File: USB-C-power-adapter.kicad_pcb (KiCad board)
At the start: 2 copper layers, 21.1 x 40.1 mm, 60 parts, among them J1 USB-C_GCT_USB4105-GF-A, J2 JST_SH_1x4_SM04B-SRSS-TB-LF-SN, J4 Molex_Nano-Fit_1x2_105313-220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, Q1 SQS401EN-T1_BE3, U1 TPD4E02B04DQA, U2 SIC477ED-T1-GE3, U3 STUSB4500_QFN, U4 TPD4E02B04DQA

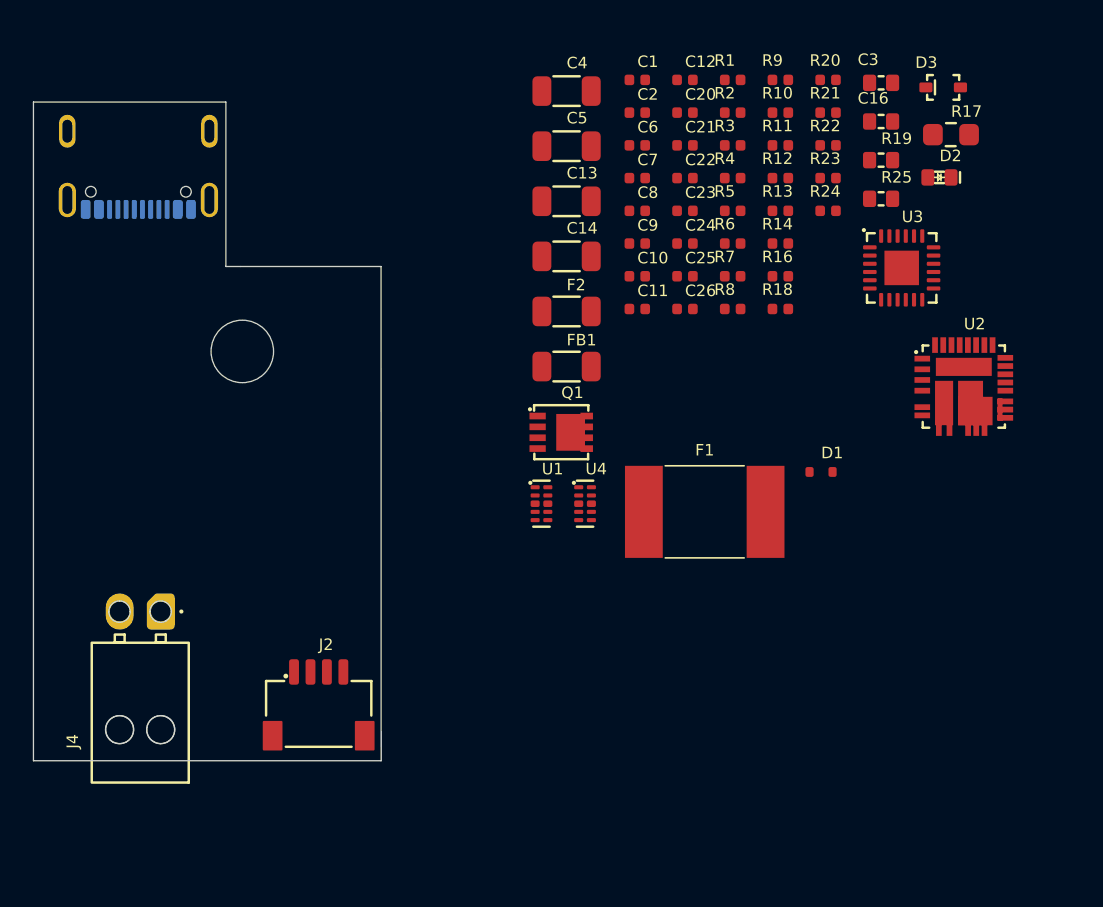
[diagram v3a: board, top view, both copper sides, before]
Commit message: [#57225] Placement of buck converter
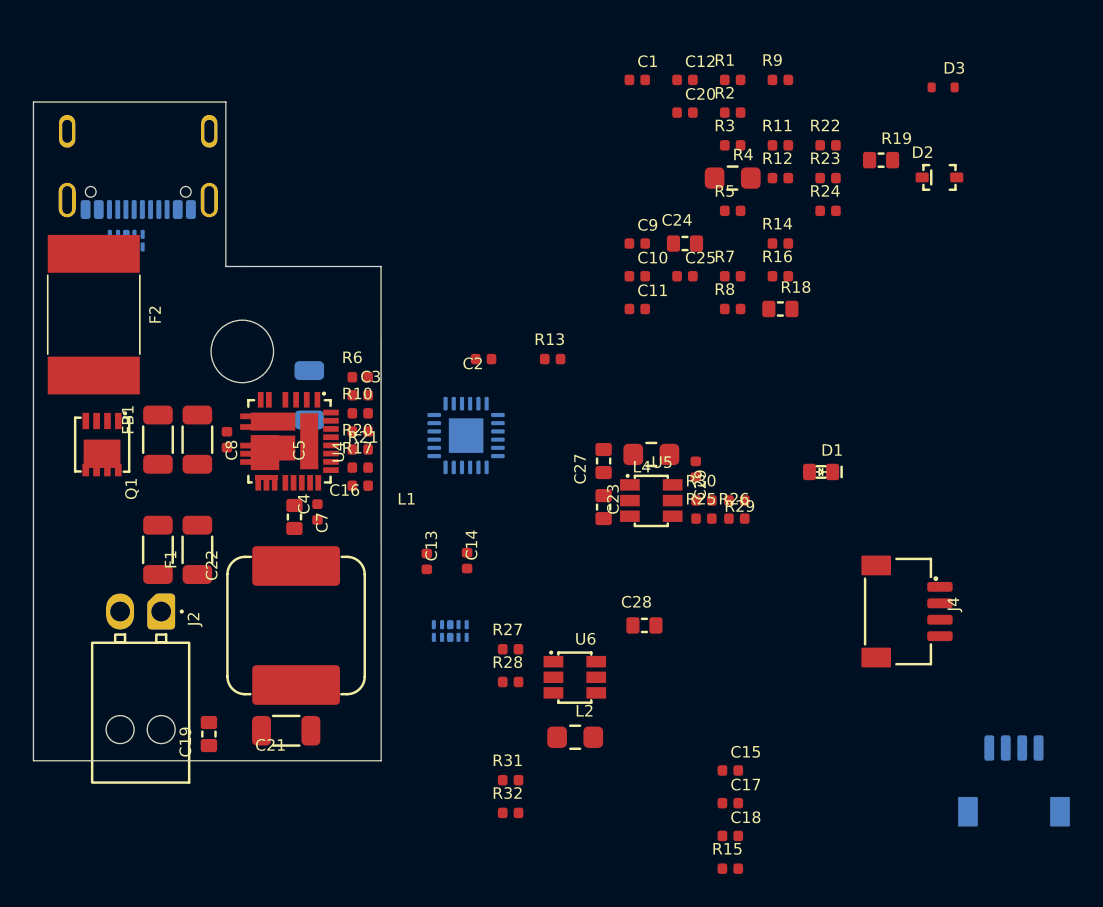
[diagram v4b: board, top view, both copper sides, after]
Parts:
- removed C26: C_1u_0402, antmicro-footprints:C_0402_1005Metric
- added C15: C_1u_0402, antmicro-footprints:C_0402_1005Metric, F.Cu at (123.9, 101.7)
- added C17: C_1n2_50V_0402, antmicro-footprints:C_0402_1005Metric, F.Cu at (123.9, 103.7)
- added C18: C_100n_0402, antmicro-footprints:C_0402_1005Metric, F.Cu at (123.9, 105.7)
- added C19: C_10u_25V_0603, antmicro-footprints:C_0603_1608Metric, F.Cu at (92.2, 99.5)
- added C27: C_10u_25V_0603, antmicro-footprints:C_0603_1608Metric, F.Cu at (116.2, 82.9)
- added C28: C_10u_25V_0603, antmicro-footprints:C_0603_1608Metric, F.Cu at (118.7, 92.9)
- added C29: C_100n_50V_X8L_0402, antmicro-footprints:C_0402_1005Metric, F.Cu at (121.8, 83.4)
- added J3: USB-C_GCT_USB4105-GF-A, antmicro-footprints:USB-C_Receptacle_GCT_USB4105-GF-A, B.Cu at (87.9, 64.1)
- added L1: L_3u3_9.2A_Vishay-IHLP-3232DZ-01, antmicro-footprints:L_Vishay-IHLP3232DZ, F.Cu at (97.5, 92.9)
- added L2: L_3u3_0.9A_0805, antmicro-footprints:L_0805_2012Metric, F.Cu at (114.5, 99.7)
- added L4: L_3u3_0.9A_0805, antmicro-footprints:L_0805_2012Metric, F.Cu at (119.1, 82.5)
- added R15: R_3R3_0402, antmicro-footprints:R_0402_1005Metric, F.Cu at (123.9, 107.7)
- added R26: R_1k3_0402, antmicro-footprints:R_0402_1005Metric, F.Cu at (124.3, 86.4)
- added R27: R_template_name_0402, antmicro-footprints:R_0402_1005Metric, F.Cu at (110.5, 94.3)
- added R28: R_680R_0402, antmicro-footprints:R_0402_1005Metric, F.Cu at (110.5, 96.3)
- added R29: R_215k_0402, antmicro-footprints:R_0402_1005Metric, F.Cu at (124.3, 85.3)
- added R30: R_30R_0402, antmicro-footprints:R_0402_1005Metric, F.Cu at (122.3, 85.3)
- added R31: R_215k_0402, antmicro-footprints:R_0402_1005Metric, F.Cu at (110.5, 102.3)
- added R32: R_30R_0402, antmicro-footprints:R_0402_1005Metric, F.Cu at (110.5, 104.3)
- added U5: AP62301WU-7, antmicro-footprints:TSOT23-6, F.Cu at (119.1, 85.3)
- added U6: AP62301WU-7, antmicro-footprints:TSOT23-6, F.Cu at (114.5, 96.0)
- C10: value C_270p_25V_0402 -> C_100n_0402
- C11, C9: value C_1n2_50V_0402 -> C_1u_0402
- C12: value C_100n_0402 -> C_1u_0402
- C13: value C_47u_16V_1206 -> C_100n_0402; footprint antmicro-footprints:C_1206_3216Metric -> antmicro-footprints:C_0402_1005Metric
- C14: value C_47u_16V_1206 -> C_1n2_50V_0402; footprint antmicro-footprints:C_1206_3216Metric -> antmicro-footprints:C_0402_1005Metric
- C16: value C_10u_25V_0603 -> C_270p_25V_0402; footprint antmicro-footprints:C_0603_1608Metric -> antmicro-footprints:C_0402_1005Metric
- C2: value C_1u_0402 -> C_4u7_25V_0402
- C20: value C_1u_0402 -> C_100n_50V_X8L_0402
- C21, C22: value C_1u_0402 -> C_47u_16V_1206; footprint antmicro-footprints:C_0402_1005Metric -> antmicro-footprints:C_1206_3216Metric
- C23: value C_100n_0402 -> C_10u_25V_0603; footprint antmicro-footprints:C_0402_1005Metric -> antmicro-footprints:C_0603_1608Metric
- C24: value C_4u7_25V_0402 -> C_10u_25V_0603; footprint antmicro-footprints:C_0402_1005Metric -> antmicro-footprints:C_0603_1608Metric
- C3: value C_4u7_0603 -> C_1u_0402; footprint antmicro-footprints:C_0603_1608Metric -> antmicro-footprints:C_0402_1005Metric
- C4: value C_10u_1206_50V -> C_4u7_0603; footprint antmicro-footprints:C_1206_3216Metric -> antmicro-footprints:C_0603_1608Metric
- C6: value C_33n_0402 -> C_10u_1206_50V; footprint antmicro-footprints:C_0402_1005Metric -> antmicro-footprints:C_1206_3216Metric; moved to B.Cu
- C7: value C_100n_50V_0402 -> C_33n_0402
- C8: value C_100n_0402 -> C_100n_50V_0402
- D1: value ESD5B5_0ST1G -> LED_G_0603_LG_L29K-G2J1-24-Z; footprint antmicro-footprints:SOD-523_NP -> antmicro-footprints:LED_0603_1608Metric_G
- D2: value LED_G_0603_LG_L29K-G2J1-24-Z -> PMEG6002EJ,115; footprint antmicro-footprints:LED_0603_1608Metric_G -> antmicro-footprints:D_SOD-323F
- D3: value PMEG6002EJ,115 -> ESD5B5_0ST1G; footprint antmicro-footprints:D_SOD-323F -> antmicro-footprints:SOD-523_NP
- F1: value F_5A_2920 -> F_7A_1206; footprint antmicro-footprints:2920-fuse -> antmicro-footprints:F_1206_3216Metric
- F2: value F_7A_1206 -> F_5A_2920; footprint antmicro-footprints:F_1206_3216Metric -> antmicro-footprints:2920-fuse
- FB1: value FB_10Z_10A_1206 -> FB_10Z_10A_WE-MPSB_1206
- J1: value USB-C_GCT_USB4105-GF-A -> JST_SH_1x4_SM04B-SRSS-TB-LF-SN; footprint antmicro-footprints:USB-C_Receptacle_GCT_USB4105-GF-A -> antmicro-footprints:Conn_JST_SH_1x4_SM04B-SRSS-TB-LF-SN
- J2: value JST_SH_1x4_SM04B-SRSS-TB-LF-SN -> Molex_Nano-Fit_1x2_105313-2202_Horizontal; footprint antmicro-footprints:Conn_JST_SH_1x4_SM04B-SRSS-TB-LF-SN -> antmicro-footprints:Conn_Molex_Nano-Fit_1x2_105313-2202_Horizontal
- J4: value Molex_Nano-Fit_1x2_105313-2202_Horizontal -> JST_SH_1x4_SM04B-SRSS-TB-LF-SN; footprint antmicro-footprints:Conn_Molex_Nano-Fit_1x2_105313-2202_Horizontal -> antmicro-footprints:Conn_JST_SH_1x4_SM04B-SRSS-TB-LF-SN
- R10: value R_3R3_0402 -> R_26k7_0402
- R11: value R_8k66_0402 -> R_0R_0402
- R12: value R_316k_0402 -> R_0R_0402
- R13: value R_140k_0.1%_0402 -> R_0R_0402
- R14: value R_10k_0.1%_0402 -> R_100k_0402
- R16: value R_2k2_0402 -> R_8k66_0402
- R17: value R_4k7_0805 -> R_316k_0402; footprint antmicro-footprints:R_0805_2012Metric -> antmicro-footprints:R_0402_1005Metric
- R18: value R_10k_0402 -> R_470R_0603; footprint antmicro-footprints:R_0402_1005Metric -> antmicro-footprints:R_0603_1608Metric
- R19: value R_470R_0603 -> R_3k9_0603
- R20: value R_0R_0402 -> R_140k_0.1%_0402
- R21: value R_0R_0402 -> R_10k_0.1%_0402
- R25: value R_3k9_0603 -> R_6k8_0402; footprint antmicro-footprints:R_0603_1608Metric -> antmicro-footprints:R_0402_1005Metric
- R3: value R_2k_0402 -> R_2k2_0402
- R4: value R_0R_0402 -> R_4k7_0805; footprint antmicro-footprints:R_0402_1005Metric -> antmicro-footprints:R_0805_2012Metric
- R5: value R_60k4_0402 -> R_10k_0402
- R6: value R_100k_0402 -> R_2k_0402
- R7: value R_26k7_0402 -> R_0R_0402
- R8: value R_0R_0402 -> R_60k4_0402
- U1, U3: moved to B.Cu
- U2: value SIC477ED-T1-GE3 -> TPD4E02B04DQA; footprint antmicro-footprints:SIC47XED-T1-GE3 -> antmicro-footprints:USON-10_2.5x1mm_P0.5mm; moved to B.Cu
- U4: value TPD4E02B04DQA -> SIC477ED-T1-GE3; footprint antmicro-footprints:USON-10_2.5x1mm_P0.5mm -> antmicro-footprints:SIC47XED-T1-GE3
- moved J1 65.8 mm to (141.2, 102.8), turned to 180 degrees
- moved U2 51.7 mm to (87.2, 69.5), turned to -90 degrees
- moved J4 44.9 mm to (134.2, 92.0)
- moved C21 43.1 mm to (96.9, 99.3), turned to 180 degrees
- moved R17 41.2 mm to (101.4, 83.3)
- moved C16 38.6 mm to (101.4, 84.4), turned to 180 degrees
- moved C22 37.3 mm to (91.5, 88.3), turned to -90 degrees
- moved C3 36.9 mm to (101.4, 78.9)
- moved R20 36.3 mm to (101.4, 82.2)
- moved R21 34.4 mm to (101.4, 81.1), turned to 180 degrees
- moved F1 33.3 mm to (89.1, 88.3), turned to -90 degrees
- moved R10 31.4 mm to (101.4, 80.0)
- moved C4 30.7 mm to (97.4, 86.3), turned to -90 degrees
- moved F2 28.7 mm to (85.2, 74.0), turned to -90 degrees
- moved C5 28.7 mm to (91.5, 81.6), turned to -90 degrees
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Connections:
- C10 pad 1: Net-(C10-Pad1) -> GND
- C10 pad 2: GND -> Net-(U3-VSYS)
- C11 pad 1: /12V_SNS -> GND
- C11 pad 2: 12V0 -> Net-(U3-VREG_1V2)
- C12 pad 1: 12V0 -> GND
- C12 pad 2: GND -> VBUS
- C13 pad 1: GND -> Net-(C13-Pad1)
- C13 pad 2: 12V0 -> Net-(U4-BOOT)
- C14 pad 1: GND -> Net-(U4-V_{SNS})
- C14 pad 2: 12V0 -> /12V_SNS
- C16 pad 1: GND -> Net-(C16-Pad1)
- C16 pad 2: 12V0 -> GND
- C2 pad 1: /VDD_12V_DCDC -> GND
- C2 pad 2: GND -> VBUS
- C20 pad 1: GND -> Net-(C20-Pad1)
- C20 pad 2: Net-(U3-VREG_2V7) -> VCC
- C21 pad 2: Net-(U3-VREG_1V2) -> 12V0
- C22 pad 2: VBUS -> 12V0
- C23 pad 2: Net-(U3-VSYS) -> 12V0
- C24 pad 2: VBUS -> 12V0
- C25 pad 1: Net-(C25-Pad1) -> Net-(U6-SW)
- C25 pad 2: VCC -> Net-(U6-BST)
- C3 pad 1: /VDRV_12V_DCDC -> /VDD_12V_DCDC
- C4 pad 1: Net-(U2-V_{CIN}) -> /VDRV_12V_DCDC
- C5 pad 1: Net-(U2-V_{CIN}) -> Net-(U4-V_{CIN})
- C6 pad 1: /12V_SS -> Net-(U4-V_{CIN})
- C7 pad 1: Net-(U2-V_{CIN}) -> /12V_SS
- C8 pad 1: Net-(C8-Pad1) -> Net-(U4-V_{CIN})
- C8 pad 2: Net-(U2-BOOT) -> GND
- C9 pad 1: Net-(U2-V_{SNS}) -> GND
- C9 pad 2: /12V_SNS -> Net-(U3-VREG_2V7)
- D1 pad 1: GND -> Net-(D1-Pad1)
- D1 pad 2: 12V0 -> GND
- F1 pad 1: Net-(F1-Pad1) -> +12V
- F1 pad 2: VBUS -> Net-(F1-Pad2)
- F2 pad 1: +12V -> Net-(F2-Pad1)
- F2 pad 2: Net-(F2-Pad2) -> VBUS
- FB1 pad 2: Net-(U2-V_{CIN}) -> Net-(U4-V_{CIN})
- J2 pad 1: GND -> Net-(F1-Pad2)
- J2 pad 2: +3V3 -> GND
- J4 pad 1: Net-(F2-Pad2) -> GND
- J4 pad 2: GND -> 3V3
- R1 pad 1: /I2C.SCL -> /Connectors/I2C.SCL
- R10 pad 1: Net-(C8-Pad1) -> /12V_FSW
- R10 pad 2: Net-(R10-Pad2) -> GND
- R11 pad 1: Net-(L1-Pad1) -> GND
- R11 pad 2: /12V_SNS -> Net-(U3-VSYS)
- R12 pad 1: Net-(U2-COMP) -> Net-(U3-VSYS)
- R12 pad 2: Net-(C10-Pad1) -> +3V3
- R13 pad 1: Net-(U2-V_{FB}) -> Net-(U4-V_{SNS})
- R14 pad 1: GND -> PWR_GOOD
- R14 pad 2: Net-(U2-V_{FB}) -> /VDD_12V_DCDC
- R16 pad 1: Net-(D2-Pad1) -> Net-(L1-Pad1)
- R16 pad 2: +12V -> /12V_SNS
- R17 pad 1: Net-(U3-DISCH) -> Net-(U4-COMP)
- R17 pad 2: VCC -> Net-(C16-Pad1)
- R18 pad 1: Net-(U3-RESET) -> Net-(C15-Pad2)
- R18 pad 2: GND -> VBUS
- R19 pad 1: Net-(C26-Pad2) -> /VBUS_DISCH
- R19 pad 2: VBUS -> Net-(C15-Pad2)
- R2 pad 1: /I2C.SDA -> /Connectors/I2C.SDA
- R20 pad 1: Net-(U3-VSYS) -> Net-(U4-V_{FB})
- R20 pad 2: +3V3 -> 12V0
- R21 pad 2: Net-(U3-VSYS) -> Net-(U4-V_{FB})
- R24 pad 2: Net-(C25-Pad1) -> Net-(C20-Pad1)
- R25 pad 1: /VBUS_DISCH -> 5V0
- R25 pad 2: Net-(C26-Pad2) -> Net-(U5-FB)
- R3 pad 1: /12V_MODE -> Net-(D1-Pad1)
- R3 pad 2: GND -> +12V
- R4 pad 1: /VDD_12V_DCDC -> Net-(U3-DISCH)
- R4 pad 2: /12V_ILIM -> VCC
- R5 pad 1: /12V_ILIM -> Net-(U3-RESET)
- R6 pad 1: Net-(U2-EN) -> /12V_MODE
- R6 pad 2: Net-(U2-V_{CIN}) -> GND
- R7 pad 1: /12V_FSW -> /VDD_12V_DCDC
- R7 pad 2: GND -> /12V_ILIM
- R8 pad 1: Net-(U2-V_{SNS}) -> /12V_ILIM
- R8 pad 2: 12V0 -> GND
- R9 pad 1: PWR_GOOD -> Net-(U4-EN)
- R9 pad 2: /VDD_12V_DCDC -> Net-(U4-V_{CIN})
- U1 pad 2: /I2C.SDA -> /Connectors/I2C.SDA
- U1 pad 4: /I2C.SCL -> /Connectors/I2C.SCL
- U1 pad 7: /I2C.SCL -> /Connectors/I2C.SCL
- U1 pad 9: /I2C.SDA -> /Connectors/I2C.SDA
- U2 pad 1: Net-(U2-V_{CIN}) -> VBUS
- U2 pad 10: GND -> VBUS
- U2 pad 2: PWR_GOOD -> /Connectors/USB.CC1
- U2 pad 3: Net-(U2-EN) -> GND
- U2 pad 4: Net-(U2-BOOT) -> /Connectors/USB.CC2
- U2 pad 5: Net-(R10-Pad2) -> unconnected-(U2-Pad5)
- U2 pad 6: Net-(R10-Pad2) -> unconnected-(U2-Pad5)
- U2 pad 7: Net-(U2-V_{CIN}) -> /Connectors/USB.CC2
- U2 pad 8: Net-(U2-V_{CIN}) -> GND
- U2 pad 9: GND -> /Connectors/USB.CC1
- U4 pad 1: VBUS -> Net-(U4-V_{CIN})
- U4 pad 10: VBUS -> GND
- U4 pad 2: /USB.CC1 -> PWR_GOOD
- U4 pad 3: GND -> Net-(U4-EN)
- U4 pad 4: /USB.CC2 -> Net-(U4-BOOT)
- U4 pad 5: unconnected-(U4-Pad5) -> Net-(R15-Pad2)
- U4 pad 6: unconnected-(U4-Pad5) -> Net-(R15-Pad2)
- U4 pad 7: /USB.CC2 -> Net-(U4-V_{CIN})
- U4 pad 8: GND -> Net-(U4-V_{CIN})
- U4 pad 9: /USB.CC1 -> GND
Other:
- outline, holes or cut-outs redrawn

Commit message: [#57225] Placement
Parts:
- C1, C10, C11, C12, C15, C2, C20, C23, C24, C25, C27, C28, C29, C9, D2, J4, L2, L4, R1, R11, R12, R18, R19, R2, R22, R23, R24, R25, R26, R27, R28, R29, R30, R31, R32, R4, R5, U5, U6: moved to B.Cu
- moved R12 49.1 mm to (82.9, 87.5), turned to 180 degrees
- moved R11 49.1 mm to (82.9, 85.3)
- moved D2 48.0 mm to (89.0, 72.0), turned to 90 degrees
- moved R24 47.9 mm to (86.3, 87.7), turned to 90 degrees
- moved R23 47.8 mm to (87.4, 87.7), turned to -90 degrees
- moved R22 47.8 mm to (88.5, 87.7), turned to 90 degrees
- moved J1 44.9 mm to (99.9, 85.1), turned to -90 degrees
- moved C20 44.4 mm to (85.2, 87.7), turned to -90 degrees
- moved C12 44.3 mm to (82.9, 82.0)
- moved R19 42.5 mm to (91.4, 72.8)
- moved C15 42.3 mm to (93.3, 72.5), turned to 90 degrees
- moved R15 40.7 mm to (96.7, 77.4), turned to -90 degrees
- moved R1 40.0 mm to (92.6, 84.5), turned to 90 degrees
- moved D3 39.8 mm to (104.5, 83.4)
- moved R2 39.7 mm to (91.5, 84.5), turned to 90 degrees
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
